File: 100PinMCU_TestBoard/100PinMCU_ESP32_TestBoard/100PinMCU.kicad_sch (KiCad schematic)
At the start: 28 parts, among them J1 SWD_Header_02x02, U2 STM32G491VET6, Y1 Crystal

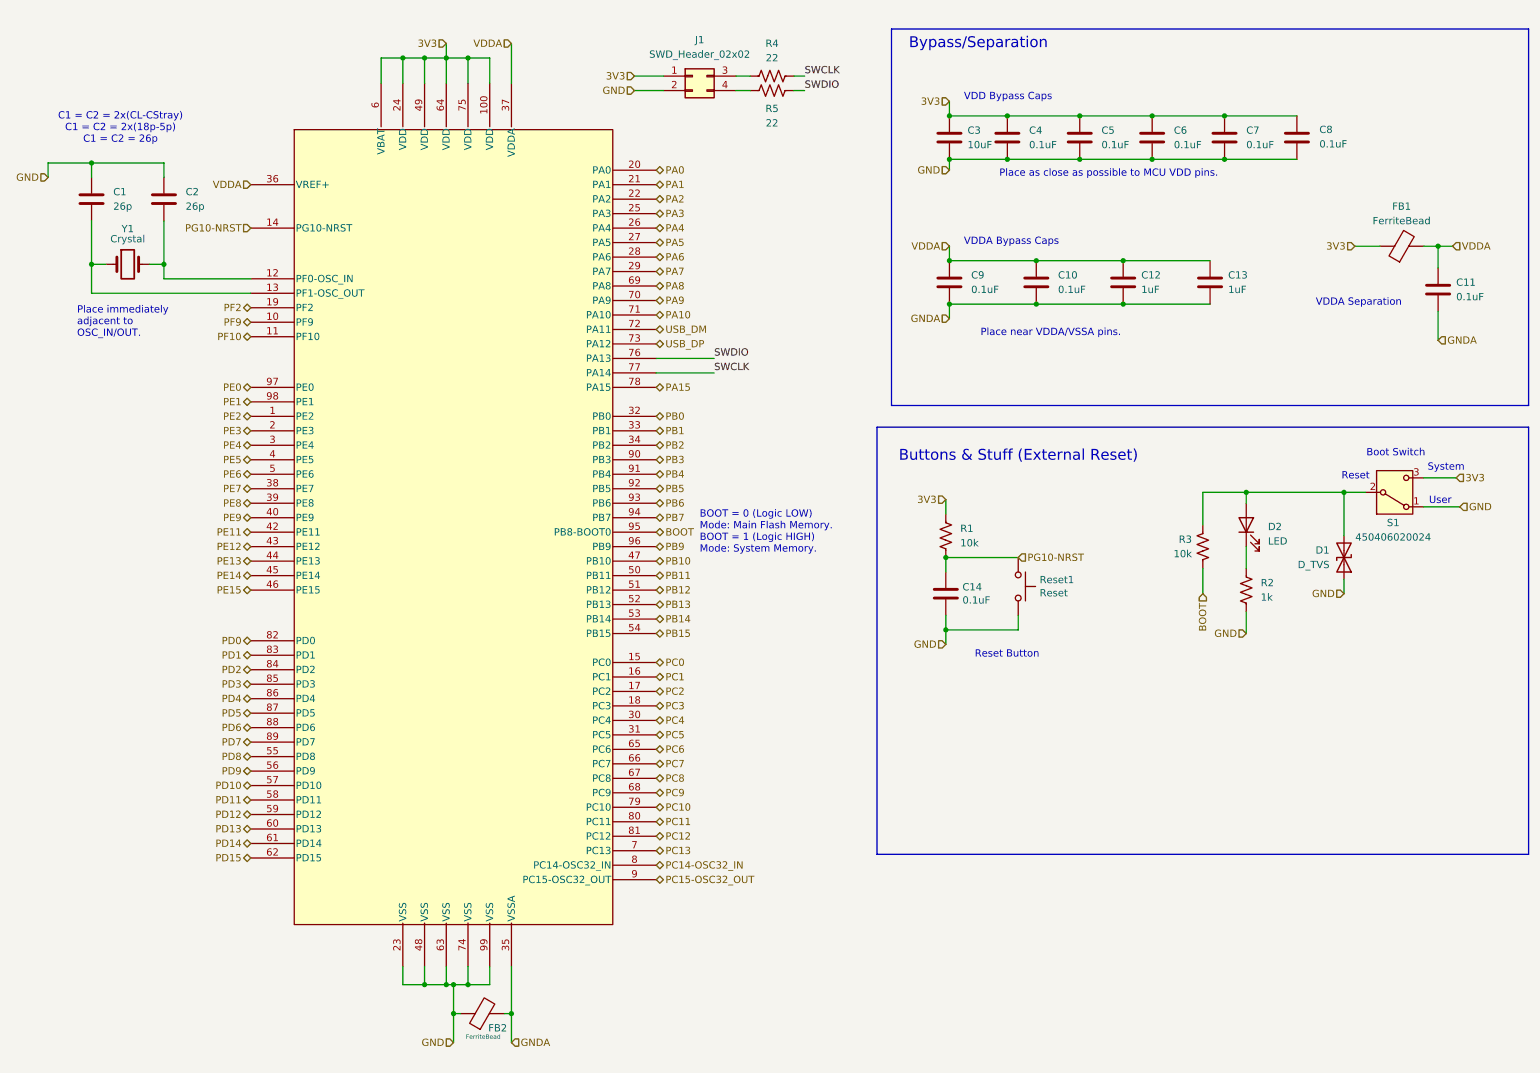
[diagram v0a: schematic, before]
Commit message: esp32 design block will be updated later
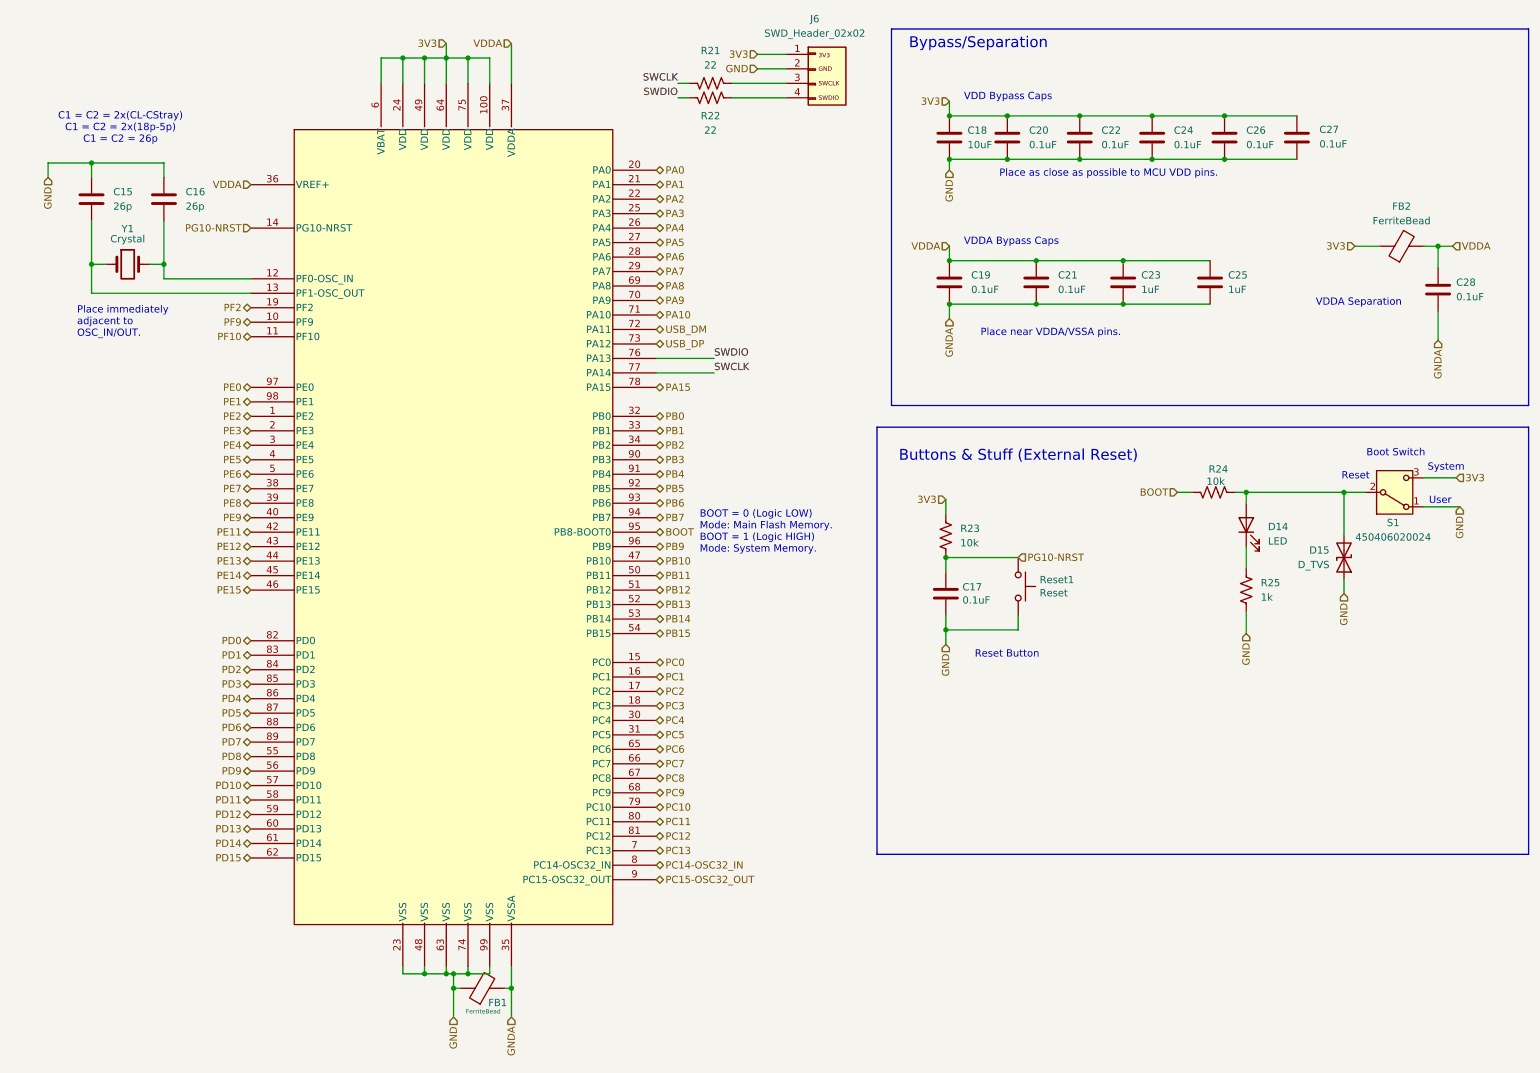
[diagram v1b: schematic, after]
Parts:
- J6: renamed from J1; LSCS P/N (none) -> C17492485
- S1: footprint 450406020024 -> 450406020024:450406020024
- U3: renamed from U2; footprint LQFP_491VET6_STM -> LQFP_491VET6_STM:LQFP_491VET6_STM
- renumbered C1 to C15, C2 to C16, C14 to C17, C3 to C18, C9 to C19, C4 to C20, C10 to C21, C5 to C22, C12 to C23, C6 to C24, C13 to C25, C7 to C26, C8 to C27, C11 to C28, D2 to D14, D1 to D15, FB2 to FB1, FB1 to FB2, R4 to R21, R5 to R22, R1 to R23, R3 to R24, R2 to R25
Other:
- moved on the sheet: FB1, R21, R22, R24

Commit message: footprints fixed
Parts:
- D14: footprint (none) -> Diode_SMD:D_0603_1608Metric_Pad1.05x0.95mm_HandSolderDiode_SMD:D_0603_1608Metric_Pad1.05x0.95mm_HandSolder
- D15: footprint Diode_SMD:D_SOD-323 -> Diode_SMD:D_SOD-323_HandSoldering
- FB1, FB2: footprint (none) -> Inductor_SMD:L_0603_1608Metric_Pad1.05x0.95mm_HandSolder
- R21, R22, R25: footprint (none) -> Resistor_SMD:R_0603_1608Metric_Pad0.98x0.95mm_HandSolder
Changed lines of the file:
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@@
 			)
 		)
-		(property "Footprint" ""
+		(property "Footprint" "Resistor_SMD:R_0603_1608Metric_Pad0.98x0.95mm_HandSolder"
 			(at 233.426 116.459 90)
 			(effects
@@
 			)
 		)
-		(property "Footprint" ""
+		(property "Footprint" "Resistor_SMD:R_0603_1608Metric_Pad0.98x0.95mm_HandSolder"
 			(at 138.684 28.321 90)
 			(effects
@@
 			)
 		)
-		(property "Footprint" ""
+		(property "Footprint" "Resistor_SMD:R_0603_1608Metric_Pad0.98x0.95mm_HandSolder"
 			(at 138.684 30.861 90)
 			(effects
@@
 			)
 		)
-		(property "Footprint" "Diode_SMD:D_SOD-323"
+		(property "Footprint" "Diode_SMD:D_SOD-323_HandSoldering"
 			(at 249.555 110.49 0)
 			(effects
@@
 			)
 		)
-		(property "Footprint" ""
+		(property "Footprint" "Inductor_SMD:L_0603_1608Metric_Pad1.05x0.95mm_HandSolder"
 			(at 98.425 187.833 90)
 			(effects
@@
 			)
 		)
-		(property "Footprint" ""
+		(property "Footprint" "Diode_SMD:D_0603_1608Metric_Pad1.05x0.95mm_HandSolderDiode_SMD:D_0603_1608Metric_Pad1.05x0.95mm_HandSolder"
 			(at 232.41 104.775 0)
 			(effects
@@
 			)
 		)
-		(property "Footprint" ""
+		(property "Footprint" "Inductor_SMD:L_0603_1608Metric_Pad1.05x0.95mm_HandSolder"
 			(at 259.715 57.658 90)
 			(effects

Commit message: footprints fixed actually
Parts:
- D14: footprint Diode_SMD:D_0603_1608Metric_Pad1.05x0.95mm_HandSolderDiode_SMD:D_0603_1608Metric_Pad1.05x0.95mm_HandSolder -> Diode_SMD:D_0603_1608Metric_Pad1.05x0.95mm_HandSolder
- J6: footprint 878320406:CONN04_878320406_MOL -> UTSVT_Connectors:CONN04_878320406_MOL
- Reset1: footprint TL3365AF180QG:TL3365AF180QG -> UTSVT_Esp32:TL3365AF180QG
- S1: footprint 450406020024:450406020024 -> UTSVT_Esp32:450406020024
- U3: footprint LQFP_491VET6_STM:LQFP_491VET6_STM -> UTSVT_ICs:LQFP_491VET6_STM
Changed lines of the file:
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@@
 			)
 		)
-		(property "Footprint" "LQFP_491VET6_STM:LQFP_491VET6_STM"
+		(property "Footprint" "UTSVT_ICs:LQFP_491VET6_STM"
 			(at 57.785 38.735 0)
 			(effects
@@
 			)
 		)
-		(property "Footprint" "Diode_SMD:D_0603_1608Metric_Pad1.05x0.95mm_HandSolderDiode_SMD:D_0603_1608Metric_Pad1.05x0.95mm_HandSolder"
+		(property "Footprint" "Diode_SMD:D_0603_1608Metric_Pad1.05x0.95mm_HandSolder"
 			(at 232.41 104.775 0)
 			(effects
@@
 			)
 		)
-		(property "Footprint" "878320406:CONN04_878320406_MOL"
+		(property "Footprint" "UTSVT_Connectors:CONN04_878320406_MOL"
 			(at 156.845 22.225 0)
 			(effects
@@
 			)
 		)
-		(property "Footprint" "450406020024:450406020024"
+		(property "Footprint" "UTSVT_Esp32:450406020024"
 			(at 280.035 4.14 0)
 			(effects
@@
 			)
 		)
-		(property "Footprint" "TL3365AF180QG:TL3365AF180QG"
+		(property "Footprint" "UTSVT_Esp32:TL3365AF180QG"
 			(at 197.485 115.57 0)
 			(effects

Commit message: lakshay comments addressed footprint p/n in progress
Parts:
- D1: renamed from D15; footprint Diode_SMD:D_SOD-323_HandSoldering -> Diode_SMD:D_SOD-323
- D2: renamed from D14; footprint Diode_SMD:D_0603_1608Metric_Pad1.05x0.95mm_HandSolder -> (none)
- FB1: renamed from FB2; footprint Inductor_SMD:L_0603_1608Metric_Pad1.05x0.95mm_HandSolder -> (none)
- FB2: renamed from FB1; footprint Inductor_SMD:L_0603_1608Metric_Pad1.05x0.95mm_HandSolder -> (none)
- J1: renamed from J6; footprint UTSVT_Connectors:CONN04_878320406_MOL -> 878320406:CONN04_878320406_MOL
- R2: renamed from R25; footprint Resistor_SMD:R_0603_1608Metric_Pad0.98x0.95mm_HandSolder -> (none)
- R4: renamed from R21; footprint Resistor_SMD:R_0603_1608Metric_Pad0.98x0.95mm_HandSolder -> (none)
- R5: renamed from R22; footprint Resistor_SMD:R_0603_1608Metric_Pad0.98x0.95mm_HandSolder -> (none)
- Reset1: footprint UTSVT_Esp32:TL3365AF180QG -> TL3365AF180QG:TL3365AF180QG
- S1: footprint UTSVT_Esp32:450406020024 -> 450406020024:450406020024
- U2: renamed from U3; footprint UTSVT_ICs:LQFP_491VET6_STM -> LQFP_491VET6_STM:LQFP_491VET6_STM
- renumbered C15 to C1, C21 to C10, C28 to C11, C23 to C12, C25 to C13, C17 to C14, C16 to C2, C18 to C3, C20 to C4, C22 to C5, C24 to C6, C26 to C7, C27 to C8, C19 to C9, R23 to R1, R24 to R3
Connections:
- net PC13: no longer names the net of U2.7 (PC13)
- net PC14-OSC32_IN: no longer names the net of U2.8 (PC14-OSC32_IN)
- net PC15-OSC32_OUT: no longer names the net of U2.9 (PC15-OSC32_OUT)
- no-connect marks 0 -> 3
